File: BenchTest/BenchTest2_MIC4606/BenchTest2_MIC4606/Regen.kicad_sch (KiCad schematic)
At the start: 11 parts, among them Q3 Q_PMOS_DGS, Q4 Q_PMOS_DGS

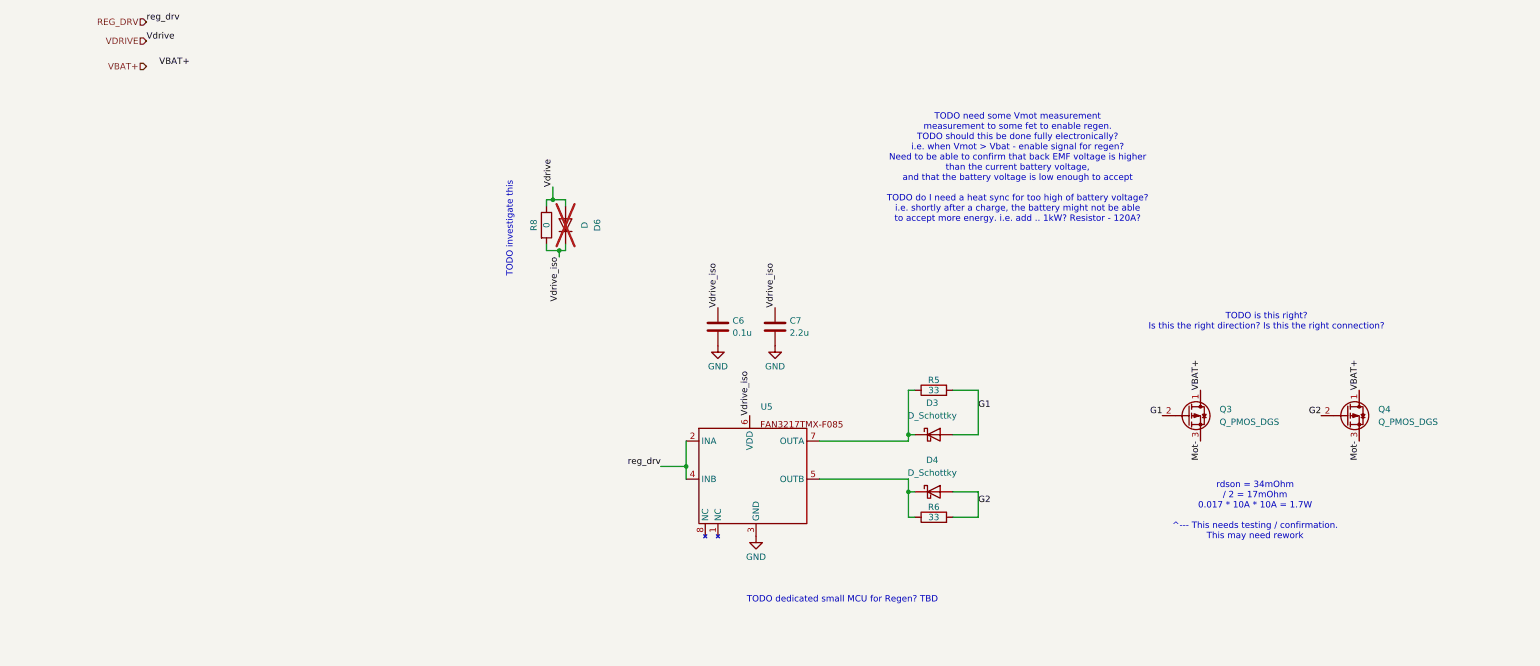
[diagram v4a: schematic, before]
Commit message: Adapting Regen to be a Regen Heater
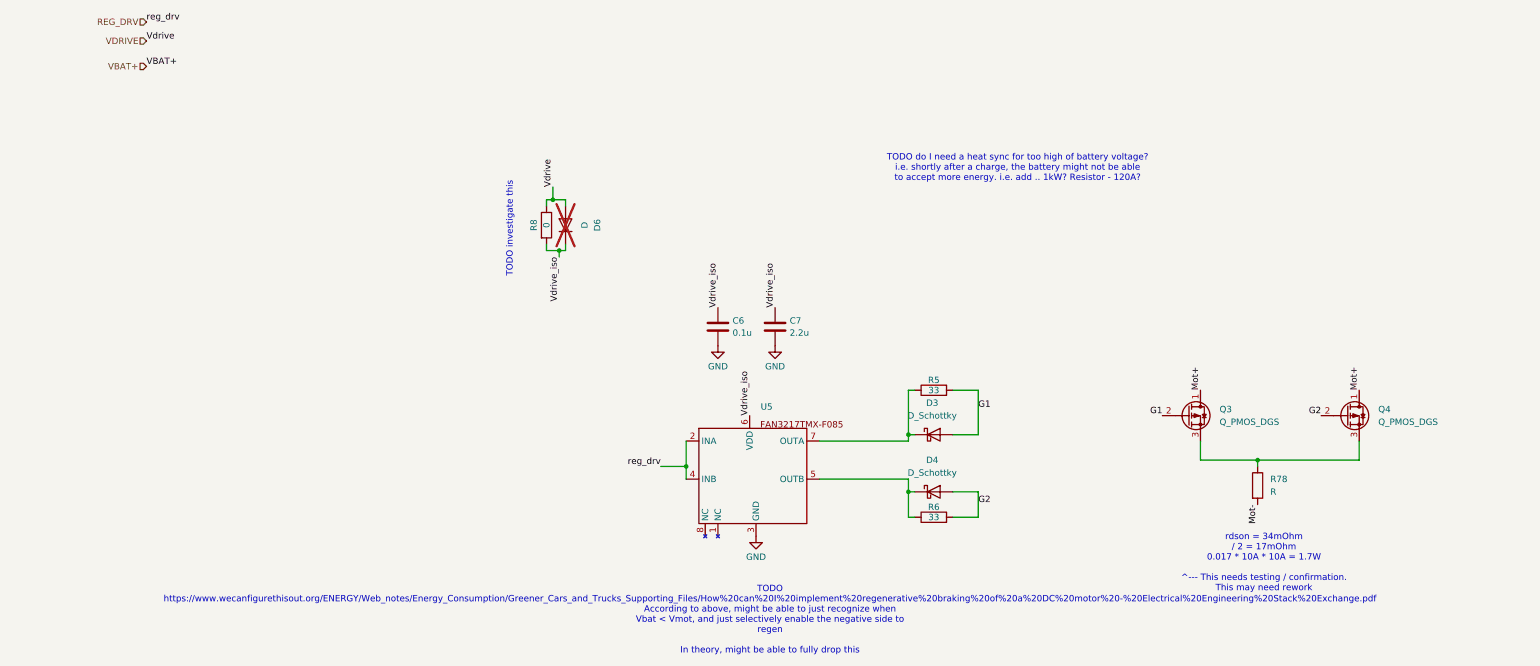
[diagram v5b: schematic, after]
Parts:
- added R78: R, symbol Device:R
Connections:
- net Mot-: now also R78.2; no longer Q3.3 (S), Q4.3 (S)
- net VBAT+: no longer Q3.1 (D), Q4.1 (D)
- new net: Q3.3 (S), Q4.3 (S), R78.1
- new net Mot+: Q3.1 (D), Q4.1 (D)
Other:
- note added: "TODO do I need a heat sync for too high of battery voltage? i.e. shortly after a charge, the battery might not be able to accept more energy. i.e. add .. 1kW? Resistor - 120A?"
- note added: "TODO https://www.wecanfigurethisout.org/ENERGY/Web_notes/Energy_Consumption/Greener_Cars_and_Trucks_Supporting_Files/How%20can%20I%20implement%20regenerative%20braking%20of%20a%20DC%20motor%20-%20Electrical%20Engineering%20Stack%20Exchange.pdf According to above, might be able to just recognize when Vbat < Vmot, and just selectively enable the negative side to regen In theory, might be able to fu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"
- note removed: "TODO dedicated small MCU for Regen? TBD"
- note removed: "TODO is this right? Is this the right direction? Is this the right connection?"
- note removed: "TODO need some Vmot measurement measurement to some fet to enable regen. TODO should this be done fully electronically? i.e. when Vmot > Vbat - enable signal for regen? Need to be able to confirm that back EMF voltage is higher than the current battery voltage, and that the battery voltage is low enough to accept TODO do I need a heat sync for too high of battery voltage? i.e. shortly after a cha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"
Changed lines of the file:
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@@
 	(generator_version "9.0")
 	(paper "A4")
-	(text "TODO need some Vmot measurement\nmeasurement to some fet to enable regen.\nTODO should this be done fully electronically? \ni.e. when Vmot > Vbat - enable signal for regen?\nNeed to be able to confirm that back EMF voltage is higher\nthan the current battery voltage,\nand that the battery voltage is low enough to accept\n\nTODO do I need a heat sync for too high of battery voltage?\ni.e. shortly after a charge, the battery might not be able\nto accept more energy. i.e. add .. 1kW? Resistor - 120A?"
+	(text "TODO do I need a heat sync for too high of battery voltage?\ni.e. shortly after a charge, the battery might not be able\nto accept more energy. i.e. add .. 1kW? Resistor - 120A?"
 		(exclude_from_sim no)
 		(at 198.374 45.72 0)
@@
 		)
 	)
-	(text "TODO is this right?\nIs this the right direction? Is this the right connection?"
-		(exclude_from_sim no)
-		(at 248.158 76.454 0)
-		(effects
-			(font
-				(size 1.27 1.27)
-			)
-		)
-	)
 	(text "TODO investigate this"
 		(exclude_from_sim no)
@@
 	(text "rdson = 34mOhm\n/ 2 = 17mOhm\n0.017 * 10A * 10A = 1.7W\n\n^--- This needs testing / confirmation.\nThis may need rework"
 		(exclude_from_sim no)
-		(at 245.872 114.3 0)
-		(effects
-			(font
-				(size 1.27 1.27)
-			)
-		)
-	)
-	(text "TODO dedicated small MCU for Regen? TBD"
-		(exclude_from_sim no)
-		(at 163.322 132.08 0)
-		(effects
-			(font
-				(size 1.27 1.27)
-			)
-		)
+		(at 247.65 124.714 0)
+		(effects
+			(font
+				(size 1.27 1.27)
+			)
+		)
+	)
+	(text "TODO\nhttps://www.wecanfigurethisout.org/ENERGY/Web_notes/Energy_Consumption/Greener_Cars_and_Trucks_Supporting_Files/How%20can%20I%20implement%20regenerative%20braking%20of%20a%20DC%20motor%20-%20Electrical%20Engineering%20Stack%20Exchange.pdf\nAccording to above, might be able to just recognize when \nVbat < Vmot, and just selectively enable the negative side to \nregen\n\nIn theory, might be able to fully drop this"
+		(exclude_from_sim no)
+		(at 148.844 136.144 0)
+		(effects
+			(font
+				(size 1.27 1.27)
+			)
+		)
+	)
+	(junction
+		(at 246.38 104.14)
+		(diameter 0)
+		(color 0 0 0 0)
 	)
 	(junction
@@
 	(wire
 		(pts
+			(xy 246.38 104.14) (xy 246.38 105.41)
+		)
+		(stroke
+			(width 0)
+			(type default)
+		)
+	)
+	(wire
+		(pts
 			(xy 106.68 62.23) (xy 106.68 63.5)
 		)
@@
 	(wire
 		(pts
+			(xy 234.95 100.33) (xy 234.95 104.14)
+		)
+		(stroke
+			(width 0)
+			(type default)
+		)
+	)
+	(wire
+		(pts
 			(xy 176.53 115.57) (xy 176.53 110.49)
 		)
@@
 	(wire
 		(pts
+			(xy 246.38 104.14) (xy 266.7 104.14)
+		)
+		(stroke
+			(width 0)
+			(type default)
+		)
+	)
+	(wire
+		(pts
 			(xy 176.53 90.17) (xy 176.53 99.06)
 		)
@@
 	(wire
 		(pts
+			(xy 266.7 104.14) (xy 266.7 100.33)
+		)
+		(stroke
+			(width 0)
+			(type default)
+		)
+	)
+	(wire
+		(pts
 			(xy 190.5 90.17) (xy 190.5 99.06)
 		)
@@
 		(pts
 			(xy 107.95 62.23) (xy 107.95 60.96)
+		)
+		(stroke
+			(width 0)
+			(type default)
+		)
+	)
+	(wire
+		(pts
+			(xy 234.95 104.14) (xy 246.38 104.14)
 		)
 		(stroke
@@
 		)
 	)
+	(label "Mot-"
+		(at 246.38 113.03 270)
+		(effects
+			(font
+				(size 1.27 1.27)
+			)
+			(justify right bottom)
+		)
+	)
 	(label "Vdrive"
 		(at 24.13 20.32 0)
@@
 	)
 	(label "VBAT+"
-		(at 234.95 90.17 90)
-		(effects
-			(font
-				(size 1.27 1.27)
-			)
-			(justify left bottom)
-		)
-	)
-	(label "VBAT+"
-		(at 26.67 25.4 0)
+		(at 24.13 25.4 0)
 		(effects
 			(font
@@
 		)
 	)
+	(label "Mot+"
+		(at 234.95 90.17 90)
+		(effects
+			(font
+				(size 1.27 1.27)
+			)
+			(justify left bottom)
+		)
+	)
 	(label "G1"
 		(at 227.33 95.25 180)
@@
 		)
 	)
-	(label "VBAT+"
+	(label "Mot+"
 		(at 266.7 90.17 90)
 		(effects
@@
 			)
 			(justify left bottom)
-		)
-	)
-	(label "Mot-"
-		(at 266.7 100.33 270)
-		(effects
-			(font
-				(size 1.27 1.27)
-			)
-			(justify right bottom)
 		)
 	)
@@
 			)
 			(justify left bottom)
-		)
-	)
-	(label "Mot-"
-		(at 234.95 100.33 270)
-		(effects
-			(font
-				(size 1.27 1.27)
-			)
-			(justify right bottom)
 		)
 	)
@@
 					(unit 1)
 				)
+			)
+		)
+	)
+	(symbol
+		(lib_id "Device:R")
+		(at 246.38 109.22 0)
+		(unit 1)
+		(exclude_from_sim no)
+		(in_bom yes)
+		(on_board yes)
+		(dnp no)
+		(fields_autoplaced yes)
+		(property "Reference" "R78"
+			(at 248.92 107.9499 0)
+			(effects
+				(font
+					(size 1.27 1.27)
+				)
+				(justify left)
+			)
+		)
+		(property "Value" "R"
+			(at 248.92 110.4899 0)
+			(effects
+				(font
+					(size 1.27 1.27)
+				)
+				(justify left)
+			)
+		)
+		(property "Footprint" ""
+			(at 244.602 109.22 90)
+			(effects
+				(font
+					(size 1.27 1.27)
+				)
+				(hide yes)
+			)
+		)
+		(property "Datasheet" "~"
+			(at 246.38 109.22 0)
+			(effects
+				(font
+					(size 1.27 1.27)
+				)
+				(hide yes)
+			)
+		)
+		(property "Description" "Resistor"
+			(at 246.38 109.22 0)
+			(effects
+				(font
+					(size 1.27 1.27)
+				)
+				(hide yes)
+			)
+		)
+		(pin "2"
+		)
+		(pin "1"
+		)
+		(instances
+			(project ""
+				(path "/5c5197d3-4aa5-4f8b-b790-1e4b8d49fd62/eb34c613-22d6-4b91-b5c9-3bbcb10d59f1"
+					(reference "R78")
+					(unit 1)
+				)

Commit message: Footprint / Capacitor Assignment
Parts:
- D3, D4, D6: footprint (none) -> Diode_SMD:D_0603_1608Metric_Pad1.05x0.95mm_HandSolder
- R8: footprint (none) -> Resistor_SMD:R_0402_1005Metric_Pad0.72x0.64mm_HandSolder
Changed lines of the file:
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@@
 			)
 		)
-		(property "Footprint" ""
+		(property "Footprint" "Diode_SMD:D_0603_1608Metric_Pad1.05x0.95mm_HandSolder"
 			(at 181.61 110.49 0)
 			(effects
@@
 			)
 		)
-		(property "Footprint" ""
+		(property "Footprint" "Diode_SMD:D_0603_1608Metric_Pad1.05x0.95mm_HandSolder"
 			(at 107.95 57.15 0)
 			(effects
@@
 			)
 		)
-		(property "Footprint" ""
+		(property "Footprint" "Resistor_SMD:R_0402_1005Metric_Pad0.72x0.64mm_HandSolder"
 			(at 102.362 57.15 90)
 			(effects
@@
 			)
 		)
-		(property "Footprint" ""
+		(property "Footprint" "Diode_SMD:D_0603_1608Metric_Pad1.05x0.95mm_HandSolder"
 			(at 181.61 99.06 0)
 			(effects
